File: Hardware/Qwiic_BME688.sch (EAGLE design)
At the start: 30 parts, among them J2 QWIIC_RA, J4 QWIIC_RA, U1 BME688LGA

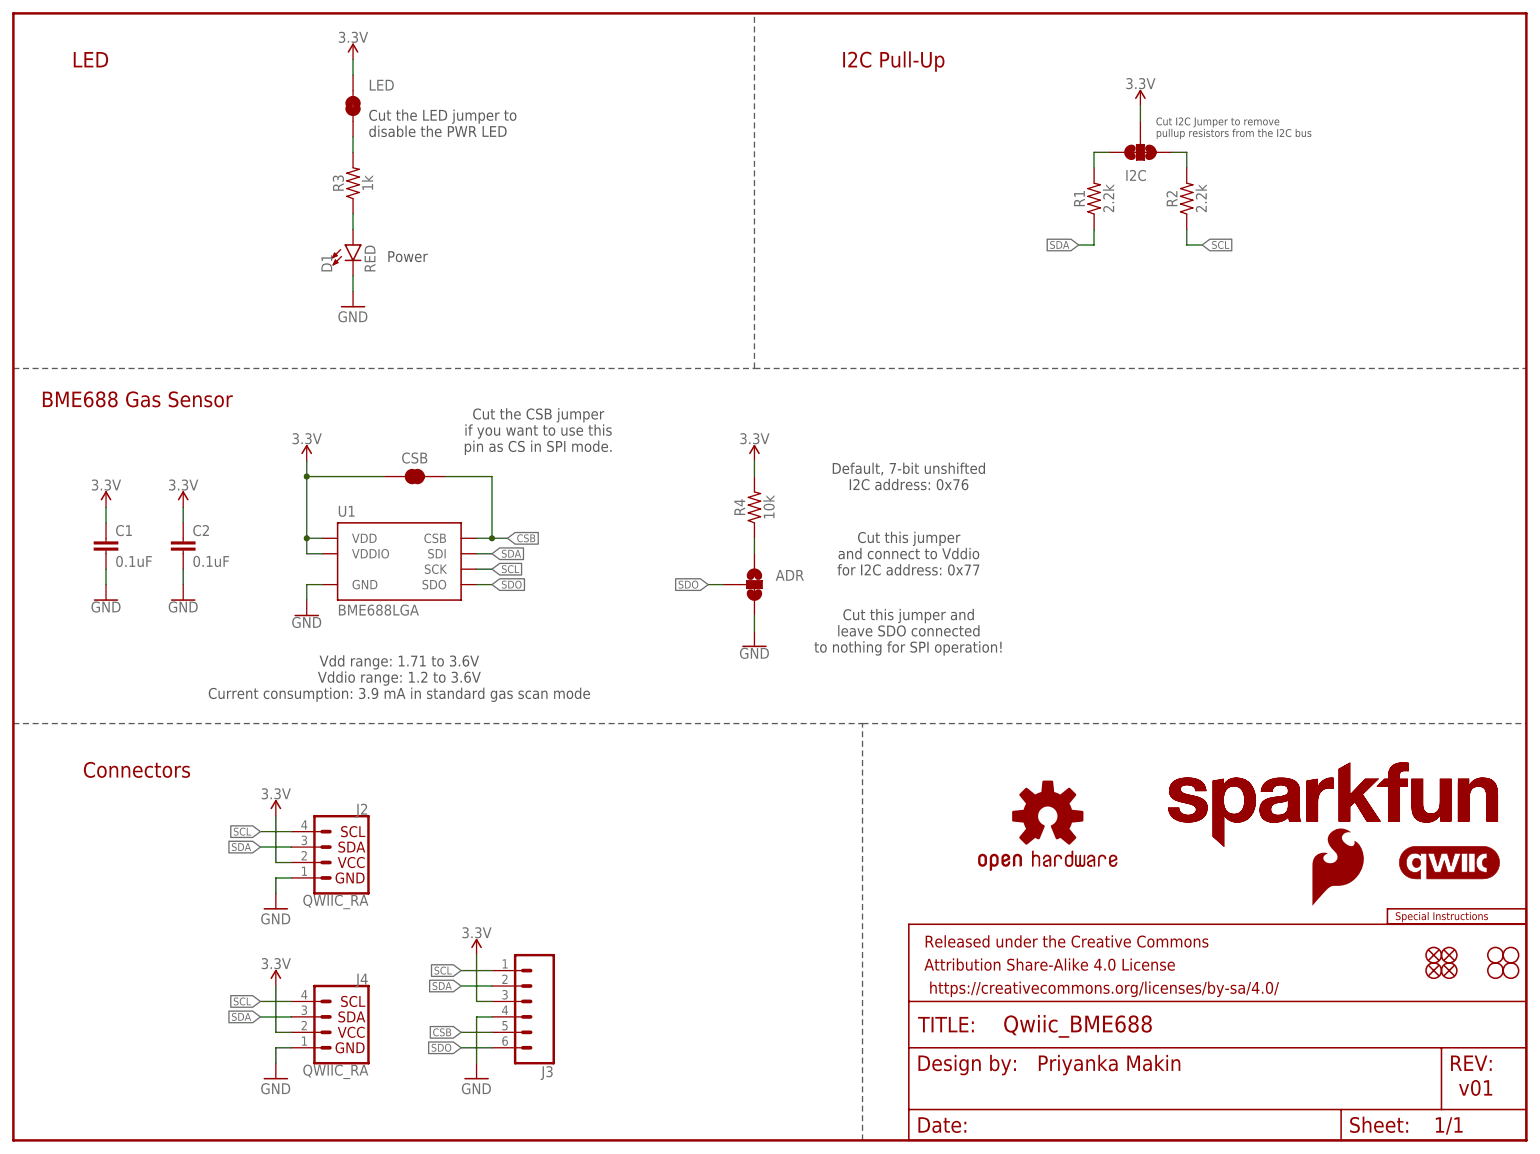
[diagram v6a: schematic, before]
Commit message: Double check
Add note clarifying configuration to SPI mode.
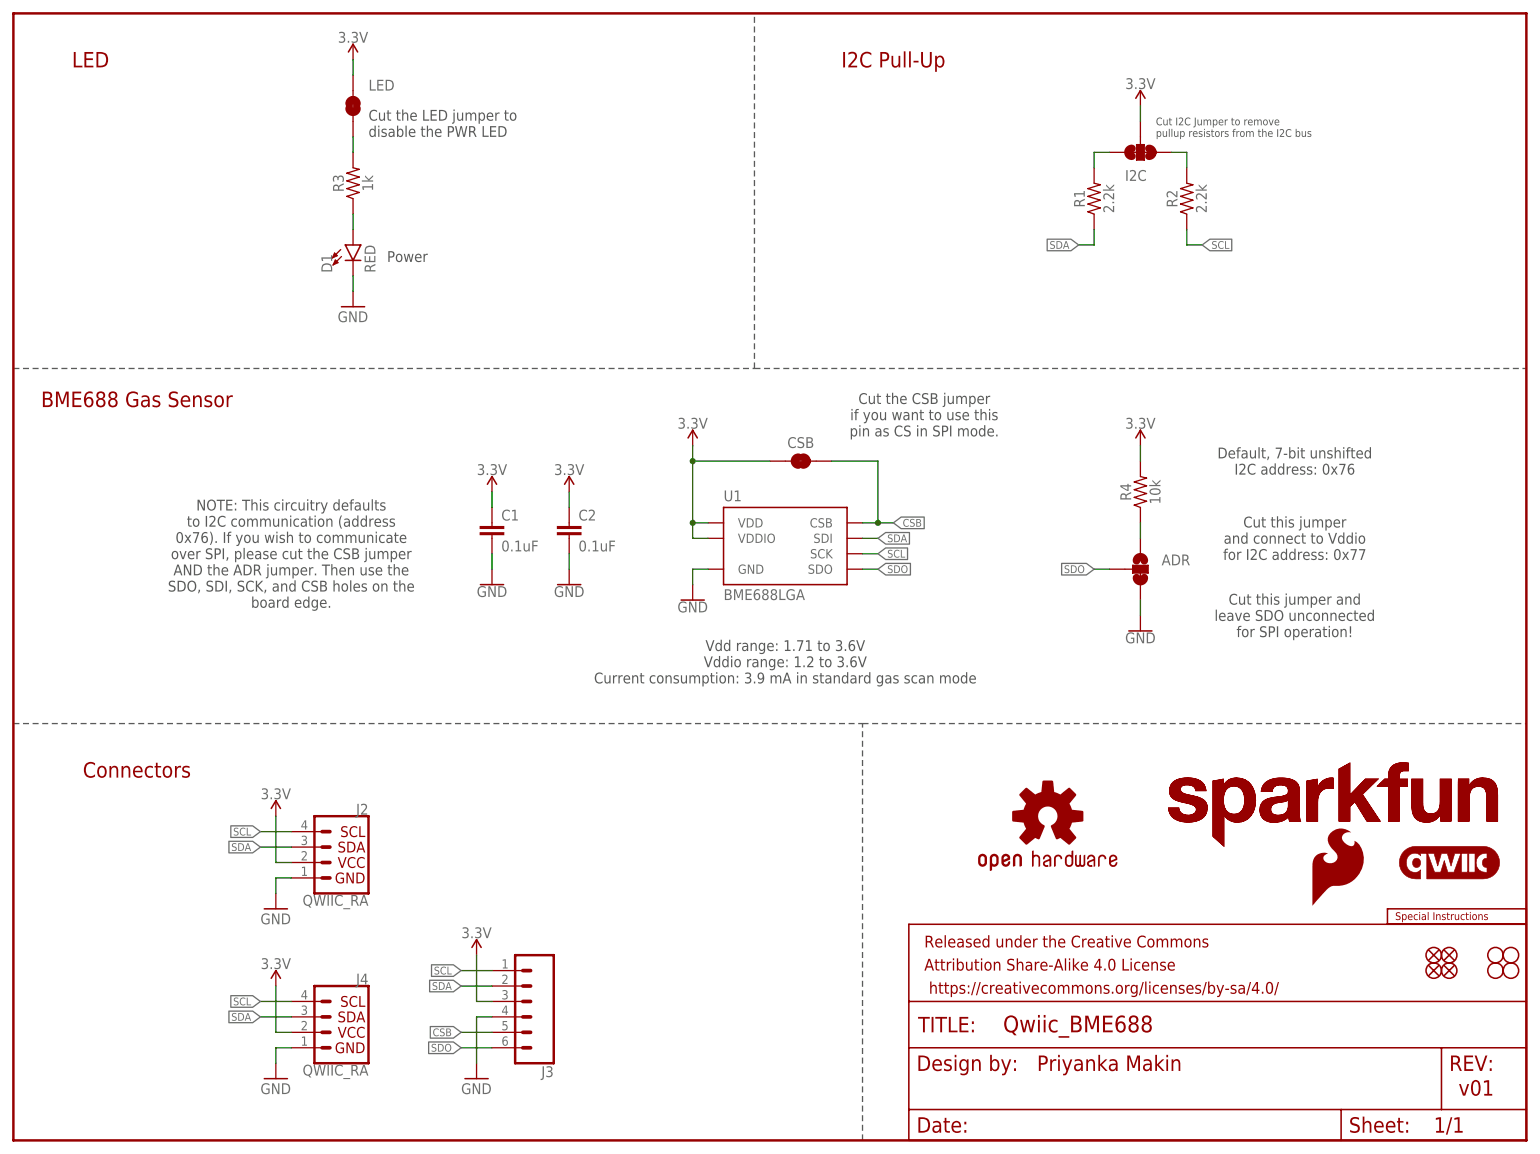
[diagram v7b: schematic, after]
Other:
- note added: "Cut this jumper and leave SDO unconnected for SPI operation!"
- note added: "NOTE: This circuitry defaults to I2C communication (address 0x76). If you wish to communicate over SPI, please cut the CSB jumper AND the ADR jumper. Then use the SDO, SDI, SCK, and CSB holes on the board edge."
- note removed: "Cut this jumper and leave SDO connected to nothing for SPI operation!"
- moved on the sheet: ADR, C1, C2, CSB, R4, U1

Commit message: Update net names
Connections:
- net SDA renamed SDA/POCI
- new net SDO/PICO: U1.SDO
- net SDO: no longer U1.SDO
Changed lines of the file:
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@@
 </segment>
 </net>
-<net name="SDA" class="0">
+<net name="SDA/POCI" class="0">
 <segment>
 <pinref part="J2" gate="G$1" pin="3"/>
@@
 <net name="SDO" class="0">
 <segment>
-<pinref part="U1" gate="U1" pin="SDO"/>
-<wire x1="139.7" y1="93.98" x2="142.24" y2="93.98" width="0.1524" layer="91"/>
-<label x="142.24" y="93.98" size="1.27" layer="95" xref="yes"/>
-</segment>
-<segment>
 <pinref part="ADR" gate="G$1" pin="2"/>
 <wire x1="180.34" y1="93.98" x2="177.8" y2="93.98" width="0.1524" layer="91"/>
@@
 </segment>
 </net>
+<net name="SDO/PICO" class="0">
+<segment>
+<pinref part="U1" gate="U1" pin="SDO"/>
+<wire x1="139.7" y1="93.98" x2="142.24" y2="93.98" width="0.1524" layer="91"/>
+<label x="142.24" y="93.98" size="1.27" layer="95" xref="yes"/>
+</segment>
+</net>
